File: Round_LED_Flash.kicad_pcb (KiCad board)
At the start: 4 copper layers, 84 x 84 mm, 65 parts, among them J1 USB4085-GF-A, J2 BATTERY, Q20 AO3401A, Q21 AO3401A, Q22 2N7002-7-F, Q23 2N7002-7-F, SW1 POWER, SW2 SHUTTER, U10 ESP32-C3-WROOM-02-N4, U6 TPS63070RNMR

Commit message: Preserve balanced supercapacitor charger draft before completion
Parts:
- removed C31, C33: 5F 2.7V, Capacitor_THT:CP_Radial_D10.0mm_P5.00mm
- removed R31, R32: 2.2k, Resistor_SMD:R_0603_1608Metric
- added C60: 4.7u 10V, Capacitor_SMD:C_0805_2012Metric, B.Cu at (130.0, 107.0)
- added C61: 2.2u 16V, Capacitor_SMD:C_0805_2012Metric, B.Cu at (126.0, 114.5)
- added Q30: AO3401A, Package_TO_SOT_SMD:SOT-23, B.Cu at (129.5, 112.0)
- added Q31: MMBT3904-7-F, Package_TO_SOT_SMD:SOT-23, B.Cu at (134.0, 113.0)
- added Q32: MMBT3904-7-F, Package_TO_SOT_SMD:SOT-23, B.Cu at (130.0, 120.0)
- added Q33: MMBT3904-7-F, Package_TO_SOT_SMD:SOT-23, F.Cu at (108.0, 134.0)
- added R52: 100k, Resistor_SMD:R_0603_1608Metric, B.Cu at (71.0, 92.0)
- added R53: 100k, Resistor_SMD:R_0603_1608Metric, B.Cu at (67.0, 103.0)
- added R60: 100k, Resistor_SMD:R_0603_1608Metric, B.Cu at (134.0, 105.0)
- added R61: 24k, Resistor_SMD:R_0603_1608Metric, B.Cu at (136.5, 109.0)
- added R62: 10k, Resistor_SMD:R_0603_1608Metric, B.Cu at (128.0, 108.5)
- added R63: 10k, Resistor_SMD:R_0603_1608Metric, B.Cu at (131.0, 115.5)
- added R64: 100k, Resistor_SMD:R_0603_1608Metric, B.Cu at (133.0, 119.0)
- added R65: 100k, Resistor_SMD:R_0603_1608Metric, F.Cu at (111.5, 137.0)
- added R66: 100k, Resistor_SMD:R_0603_1608Metric, B.Cu at (126.5, 123.0)
- added R67: 100k, Resistor_SMD:R_0603_1608Metric, B.Cu at (138.0, 111.5)
- added R68: 47k, Resistor_SMD:R_0603_1608Metric, B.Cu at (130.0, 123.0)
- added R69: 47k, Resistor_SMD:R_0603_1608Metric, F.Cu at (108.0, 137.0)
- added U30: LTC3225EDDB#TRMPBF, Package_DFN_QFN:DFN-10-1EP_2x3mm_P0.5mm_EP0.64x2.4mm, B.Cu at (133.5, 109.0)
- Q22, Q23: value 2N7002-7-F -> MMBT3904-7-F
- moved C32 13.4 mm to (128.7, 115.9)
- moved R50 2.00 mm to (71.0, 90.0)
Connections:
- Q22 pad 1: /LOGIC_PG -> /SENSE_BASE_0
- Q23 pad 1: /LOGIC_PG -> /SENSE_BASE_1

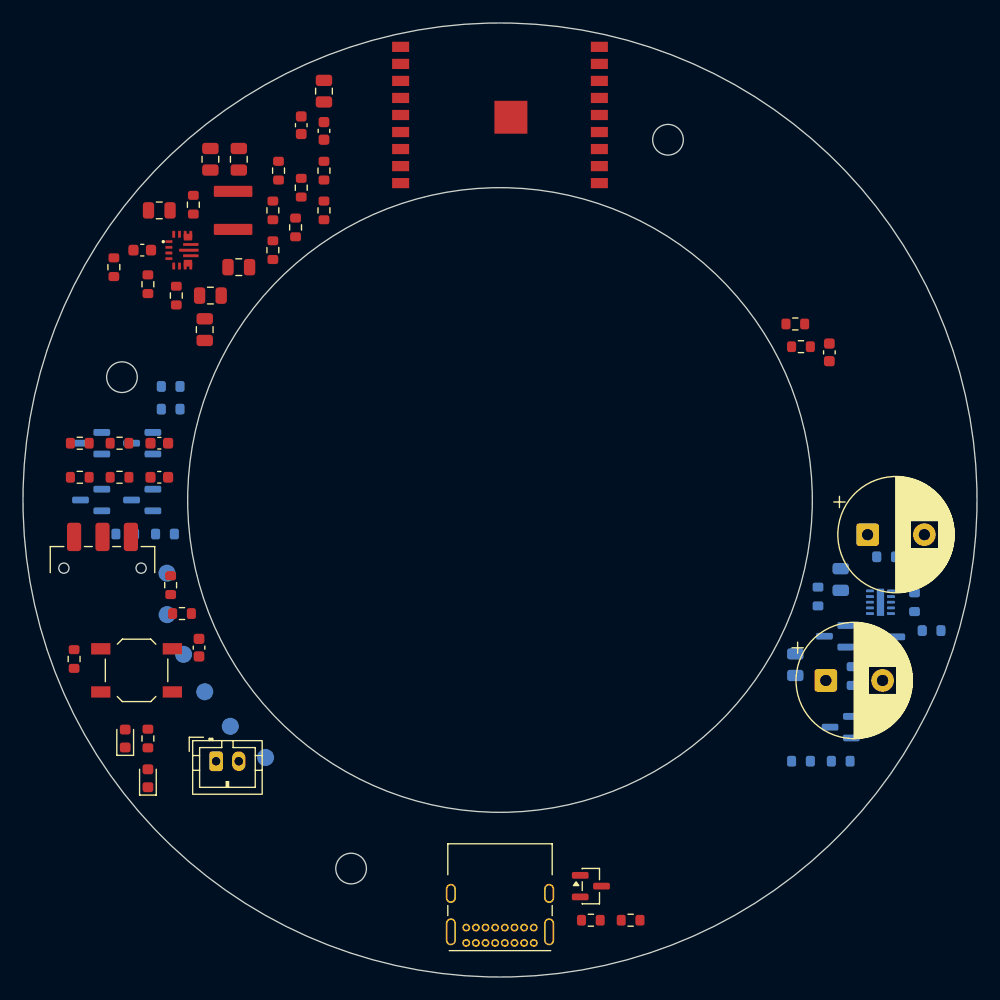
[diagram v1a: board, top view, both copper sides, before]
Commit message: Complete prototype circuit candidate with protected power and bounded flash control
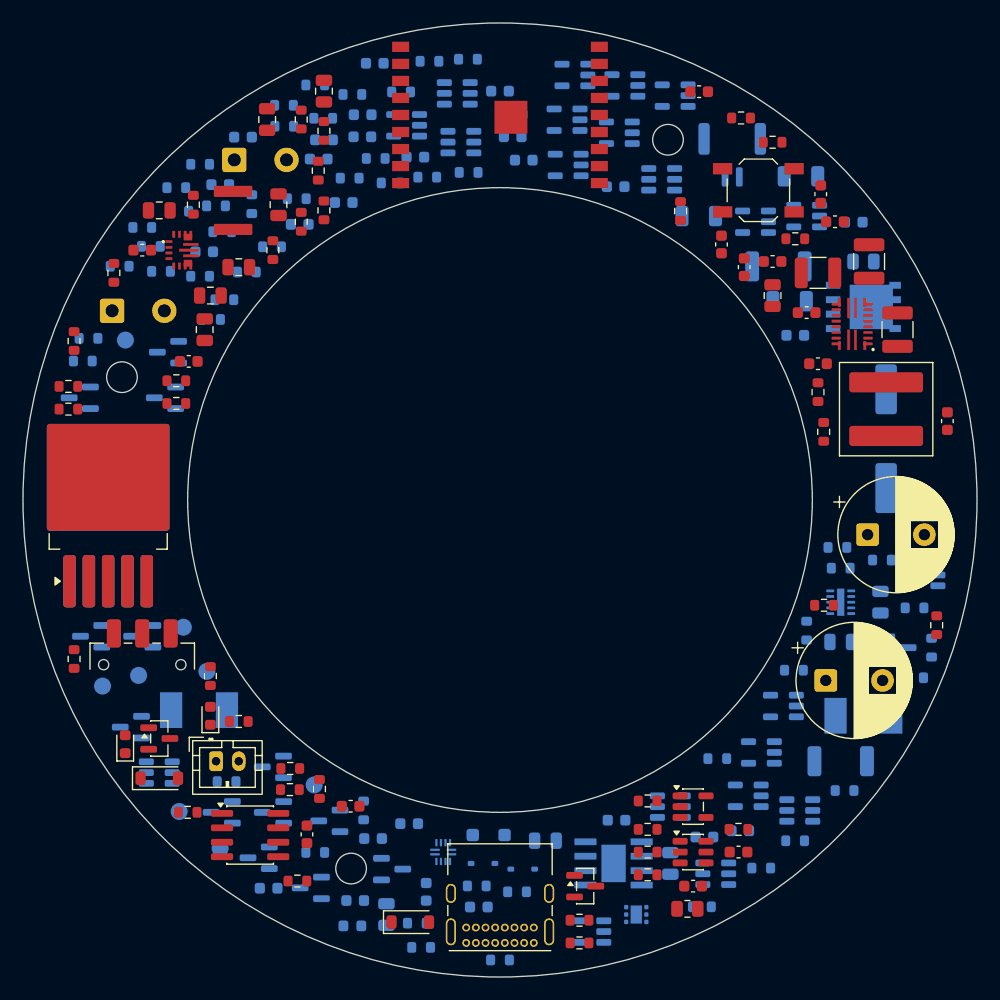
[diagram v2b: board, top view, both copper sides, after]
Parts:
- added C1: 100n, Capacitor_SMD:C_0603_1608Metric, B.Cu at (110.3, 128.2)
- added C140: 100n, Capacitor_SMD:C_0603_1608Metric, B.Cu at (84.5, 68.3)
- added C141: 100n, Capacitor_SMD:C_0603_1608Metric, B.Cu at (101.1, 68.0)
- added C142: 100n, Capacitor_SMD:C_0603_1608Metric, B.Cu at (77.4, 68.1)
- added C143: 100n, Capacitor_SMD:C_0603_1608Metric, B.Cu at (110.2, 72.4)
- added C144: 100n, Capacitor_SMD:C_0603_1608Metric, B.Cu at (89.0, 61.5)
- added C145: 100n, Capacitor_SMD:C_0603_1608Metric, B.Cu at (87.2, 135.3)
- added C146: 100n, Capacitor_SMD:C_0603_1608Metric, B.Cu at (100.0, 64.0)
- added C147: 100n, Capacitor_SMD:C_0603_1608Metric, B.Cu at (131.2, 75.5)
- added C148: 100n, Capacitor_SMD:C_0603_1608Metric, B.Cu at (98.1, 135.8)
- added C149: 100n, Capacitor_SMD:C_0603_1608Metric, B.Cu at (92.5, 69.8)
- added C150: 100n, Capacitor_SMD:C_0603_1608Metric, B.Cu at (82.4, 75.7)
- added C151: 100n, Capacitor_SMD:C_0603_1608Metric, B.Cu at (126.0, 85.5)
- added C152: 100n, Capacitor_SMD:C_0603_1608Metric, B.Cu at (118.0, 129.7)
- added C153: 100n, Capacitor_SMD:C_0603_1608Metric, B.Cu at (84.0, 70.0)
- added C155: 100n, Capacitor_SMD:C_0603_1608Metric, F.Cu at (121.0, 131.0)
- added C156: 100n, Capacitor_SMD:C_0603_1608Metric, F.Cu at (117.0, 134.0)
- added C162: 100n, Capacitor_SMD:C_0603_1608Metric, B.Cu at (86.2, 73.8)
- added C163: 100n, Capacitor_SMD:C_0603_1608Metric, B.Cu at (74.0, 78.1)
- added C2: 1u 50V, Capacitor_SMD:C_0805_2012Metric, B.Cu at (90.0, 136.5)
- added C230: 1u 10V, Capacitor_SMD:C_0603_1608Metric, B.Cu at (87.9, 68.0)
- added C231: 1u 10V, Capacitor_SMD:C_0603_1608Metric, B.Cu at (87.9, 66.1)
- added C236: 100n, Capacitor_SMD:C_0603_1608Metric, B.Cu at (102.1, 70.1)
- added C270: 22u 10V, Capacitor_SMD:C_1206_3216Metric, B.Cu at (125.5, 82.5)
- added C271: 22u 10V, Capacitor_SMD:C_1206_3216Metric, B.Cu at (126.5, 71.5)
- added C272: 22u 10V, Capacitor_SMD:C_1206_3216Metric, B.Cu at (117.5, 75.0)
- added C273: 100n, Capacitor_SMD:C_0603_1608Metric, F.Cu at (117.5, 64.0)
- added C274: 100n 50V, Capacitor_SMD:C_0603_1608Metric, F.Cu at (127.0, 83.5)
- added C275: 2.2u 10V, Capacitor_SMD:C_0805_2012Metric, F.Cu at (124.0, 82.0)
- added C276: 10n, Capacitor_SMD:C_0603_1608Metric, F.Cu at (121.5, 79.5)
- added C277: 33n, Capacitor_SMD:C_0603_1608Metric, F.Cu at (124.0, 79.0)
- added C278: 47p, Capacitor_SMD:C_0603_1608Metric, F.Cu at (129.5, 75.5)
- added C280: 10u 50V, Capacitor_SMD:C_1210_3225Metric, F.Cu at (135.0, 85.0)
- added C281: 10u 50V, Capacitor_SMD:C_1210_3225Metric, F.Cu at (132.5, 79.0)
- added C282: 10u 50V, Capacitor_SMD:C_1210_3225Metric, F.Cu at (128.0, 80.0)
- added C283: 100n 50V, Capacitor_SMD:C_0603_1608Metric, F.Cu at (128.0, 88.0)
- added C284: 120u 35V, Capacitor_SMD:CP_Elec_10x12.6, B.Cu at (134.0, 94.6)
- added C3: 1u 10V, Capacitor_SMD:C_0603_1608Metric, B.Cu at (93.5, 134.5)
- added C4: 100n, Capacitor_SMD:C_0603_1608Metric, B.Cu at (92.0, 128.5)
- added C5: 100n, Capacitor_SMD:C_0603_1608Metric, B.Cu at (79.6, 134.2)
- added C6: 4.7u 16V, Capacitor_SMD:C_0805_2012Metric, B.Cu at (115.0, 132.0)
- added C7: 100n 50V, Capacitor_SMD:C_0603_1608Metric, B.Cu at (88.8, 129.8)
- added C8: 10u 10V, Capacitor_SMD:C_0805_2012Metric, B.Cu at (104.0, 130.0)
- added C80: 100n, Capacitor_SMD:C_0603_1608Metric, B.Cu at (75.4, 72.2)
- added C9: 100n, Capacitor_SMD:C_0603_1608Metric, B.Cu at (121.2, 129.1)
- added D1: RED, LED_SMD:LED_0603_1608Metric, B.Cu at (87.0, 137.5)
- added D4: PESD5V0S1BA, Diode_SMD:D_SOD-323, B.Cu at (98.5, 132.0)
- added D5: PESD5V0S1BA, Diode_SMD:D_SOD-323, B.Cu at (102.0, 132.5)
- added D6: SMF4L6.0A, Diode_SMD:D_SOD-123F, B.Cu at (99.0, 129.5)
- added D60: 10V ZENER, Diode_SMD:D_SOD-123, F.Cu at (70.0, 124.5)
- added D70: GATE CLAMP, Diode_SMD:D_SOD-123, F.Cu at (92.1, 137.2)
- added F1: 2A FAST, Fuse:Fuse_Littelfuse-NANO2-451_453, B.Cu at (73.5, 118.5)
- added F2: 7A FAST, Fuse:Fuse_Littelfuse-NANO2-451_453, B.Cu at (132.0, 119.0)
- added J3: BM02B-GHS-TBT(LF)(SN), Connector_JST:JST_GH_BM02B-GHS-TBT_1x02-1MP_P1.25mm_Vertical, B.Cu at (120.4, 69.6)
- added J4: WARM COB, Connector_Wire:SolderWire-0.5sqmm_1x02_P4.6mm_D0.9mm_OD2.1mm, F.Cu at (65.8, 83.3)
- added J5: COOL COB, Connector_Wire:SolderWire-0.5sqmm_1x02_P4.6mm_D0.9mm_OD2.1mm, F.Cu at (76.6, 70.1)
- added L2: 1.5uH, Inductor_SMD:L_Coilcraft_XAL7030-152, F.Cu at (134.0, 92.0)
- added Q1: AO3400A, Package_TO_SOT_SMD:SOT-23, B.Cu at (80.0, 123.5)
- added Q2: AO3400A, Package_TO_SOT_SMD:SOT-23, B.Cu at (75.5, 127.5)
- added Q3: MMBT3904-7-F, Package_TO_SOT_SMD:SOT-23, B.Cu at (67.5, 120.0)
- added Q34: AO3400A, Package_TO_SOT_SMD:SOT-23, B.Cu at (70.8, 87.0)
- added Q35: MMBT3904-7-F, Package_TO_SOT_SMD:SOT-23, B.Cu at (85.0, 128.3)
- added Q60: AO4407A, Package_SO:SOIC-8_3.9x4.9mm_P1.27mm, F.Cu at (78.0, 129.5)
- added Q61: MMBT3904-7-F, Package_TO_SOT_SMD:SOT-23, F.Cu at (70.0, 121.0)
- added Q62: MMBT3904-7-F, Package_TO_SOT_SMD:SOT-23, B.Cu at (80.0, 127.5)
- added Q70: SiR800DP-T1-GE3, Package_SO:PowerPAK_SO-8_Single, B.Cu at (132.0, 83.0)
- added R1: 100, Resistor_SMD:R_0603_1608Metric, B.Cu at (75.5, 76.4)
- added R100: 4.7k, Resistor_SMD:R_0603_1608Metric, B.Cu at (83.7, 63.5)
- added R101: 4.7k, Resistor_SMD:R_0603_1608Metric, B.Cu at (125.9, 115.0)
- added R142: 165k, Resistor_SMD:R_0603_1608Metric, B.Cu at (130.0, 106.0)
- added R143: 147k, Resistor_SMD:R_0603_1608Metric, B.Cu at (133.6, 105.3)
- added R15: 2.2k, Resistor_SMD:R_0603_1608Metric, B.Cu at (77.7, 79.9)
- added R152: 100k, Resistor_SMD:R_0603_1608Metric, B.Cu at (63.8, 85.8)
- added R153: 10k, Resistor_SMD:R_0603_1608Metric, B.Cu at (81.0, 67.1)
- added R16: 22, Resistor_SMD:R_0603_1608Metric, B.Cu at (101.5, 134.5)
- added R162: 10k, Resistor_SMD:R_0603_1608Metric, B.Cu at (129.7, 104.2)
- added R163: 10k, Resistor_SMD:R_0603_1608Metric, B.Cu at (93.6, 71.6)
- added R164: 2.21M, Resistor_SMD:R_0603_1608Metric, B.Cu at (98.0, 134.0)
- added R165: 1M, Resistor_SMD:R_0603_1608Metric, B.Cu at (73.6, 70.4)
- added R17: 22, Resistor_SMD:R_0603_1608Metric, B.Cu at (100.0, 140.5)
- added R18: 10k, Resistor_SMD:R_0603_1608Metric, B.Cu at (136.5, 109.5)
- added R2: 1k, Resistor_SMD:R_0603_1608Metric, B.Cu at (69.3, 77.7)
- added R200: 137k, Resistor_SMD:R_0603_1608Metric, B.Cu at (84.4, 66.4)
- added R201: 240k, Resistor_SMD:R_0603_1608Metric, B.Cu at (86.8, 71.7)
- added R210: 357k, Resistor_SMD:R_0603_1608Metric, B.Cu at (97.2, 71.2)
- added R211: 146k, Resistor_SMD:R_0603_1608Metric, B.Cu at (87.0, 64.3)
- added R220: 100k, Resistor_SMD:R_0603_1608Metric, B.Cu at (71.8, 74.6)
- added R221: 100k, Resistor_SMD:R_0603_1608Metric, B.Cu at (93.8, 61.4)
- added R230: 2.49k, Resistor_SMD:R_0603_1608Metric, B.Cu at (91.3, 64.1)
- added R231: 2.49k, Resistor_SMD:R_0603_1608Metric, B.Cu at (136.5, 115.7)
- added R232: 4.7k, Resistor_SMD:R_0603_1608Metric, F.Cu at (72.5, 127.5)
- added R233: 2.2k, Resistor_SMD:R_0603_1608Metric, F.Cu at (81.5, 125.5)
- added R234: 2.2k, Resistor_SMD:R_0603_1608Metric, F.Cu at (77.0, 119.5)
- added R235: 100k, Resistor_SMD:R_0603_1608Metric, F.Cu at (82.2, 133.6)
- added R236: 10k, Resistor_SMD:R_0603_1608Metric, B.Cu at (90.4, 72.1)
- added R237: 10k, Resistor_SMD:R_0603_1608Metric, B.Cu at (97.2, 61.2)
- added R238: 56k, Resistor_SMD:R_0603_1608Metric, B.Cu at (75.0, 74.1)
- added R239: 261k, Resistor_SMD:R_0603_1608Metric, F.Cu at (113.0, 129.0)
- added R240: 100k, Resistor_SMD:R_0603_1608Metric, F.Cu at (113.0, 131.0)
- added R241: 10M, Resistor_SMD:R_0603_1608Metric, F.Cu at (113.0, 133.0)
- added R242: 10k, Resistor_SMD:R_0603_1608Metric, F.Cu at (121.0, 129.0)
- added R270: 0.010 0.5W, Resistor_SMD:R_0805_2012Metric, B.Cu at (132.0, 79.0)
- added R271: 162k, Resistor_SMD:R_0603_1608Metric, F.Cu at (128.0, 90.5)
- added R272: 10k, Resistor_SMD:R_0603_1608Metric, F.Cu at (128.5, 94.0)
- added R273: 1k, Resistor_SMD:R_0603_1608Metric, F.Cu at (113.0, 126.5)
- added R274: 100k, Resistor_SMD:R_0603_1608Metric, F.Cu at (107.0, 137.0)
- added R275: 120k, Resistor_SMD:R_0603_1608Metric, F.Cu at (126.0, 77.0)
- added R276: 22k 0.125W, Resistor_SMD:R_0805_2012Metric, F.Cu at (116.5, 136.0)
- added R3: 47k, Resistor_SMD:R_0603_1608Metric, B.Cu at (93.1, 139.4)
- added R4: 887k, Resistor_SMD:R_0603_1608Metric, B.Cu at (123.0, 132.4)
- added R5: 10k, Resistor_SMD:R_0603_1608Metric, B.Cu at (92.7, 137.3)
- added R6: 150k, Resistor_SMD:R_0603_1608Metric, B.Cu at (70.2, 79.9)
- added R7: 10k, Resistor_SMD:R_0603_1608Metric, B.Cu at (74.6, 84.1)
- added R70: 100k, Resistor_SMD:R_0603_1608Metric, B.Cu at (89.1, 69.9)
- added R71: 100k, Resistor_SMD:R_0603_1608Metric, B.Cu at (130.3, 125.6)
- added R72: 100 0.5W, Resistor_SMD:R_2010_5025Metric, B.Cu at (130.0, 123.0)
- added R73: 100 0.5W, Resistor_SMD:R_2010_5025Metric, B.Cu at (124.5, 79.4)
- added R8: 100k, Resistor_SMD:R_0603_1608Metric, B.Cu at (75.7, 82.4)
- added R80: 6.49k, Resistor_SMD:R_0603_1608Metric, B.Cu at (83.7, 131.0)
- added R81: 1M, Resistor_SMD:R_0603_1608Metric, B.Cu at (119.1, 122.8)
- added R82: 1M, Resistor_SMD:R_0603_1608Metric, B.Cu at (126.0, 130.0)
- added R83: 100k, Resistor_SMD:R_0603_1608Metric, B.Cu at (79.9, 77.7)
- added R84: 100k, Resistor_SMD:R_0603_1608Metric, B.Cu at (73.6, 80.3)
- added R9: 4.02k, Resistor_SMD:R_0603_1608Metric, B.Cu at (117.8, 135.8)
- added TP7: CAP_BANK, TestPoint:TestPoint_Pad_D1.5mm, B.Cu at (72.1, 111.2)
- added TP8: CAP_MID, TestPoint:TestPoint_Pad_D1.5mm, B.Cu at (67.0, 85.9)
- added U1: DW01A, Package_TO_SOT_SMD:SOT-23-6, B.Cu at (70.0, 124.0)
- added U2: TLV76033DBZR, Package_TO_SOT_SMD:SOT-23, B.Cu at (90.5, 132.5)
- added U3: TUSB320LAIRWBR, Package_DFN_QFN:Texas_X2QFN-12_1.6x1.6mm_P0.4mm, B.Cu at (95.0, 131.0)
- added U4: SN74LVC1G04DBVR, Package_TO_SOT_SMD:SOT-23-5, B.Cu at (108.0, 138.0)
- added U40: LTC6993CS6-1#TRMPBF, Package_TO_SOT_SMD:SOT-23-6, B.Cu at (114.2, 71.8)
- added U41: LTC6993CS6-1#TRMPBF, Package_TO_SOT_SMD:SOT-23-6, B.Cu at (96.6, 68.5)
- added U42: TLV3011BIDBVR, Package_TO_SOT_SMD:SOT-23-6, B.Cu at (96.2, 64.2)
- added U43: TLV3011BIDBVR, Package_TO_SOT_SMD:SOT-23-6, B.Cu at (137.4, 106.6)
- added U44: SN74LVC1G08DBVR, Package_TO_SOT_SMD:SOT-23-5, B.Cu at (122.5, 75.5)
- added U45: SN74LVC1G04DBVR, Package_TO_SOT_SMD:SOT-23-5, B.Cu at (111.0, 63.5)
- added U46: SN74LVC1G08DBVR, Package_TO_SOT_SMD:SOT-23-5, B.Cu at (110.5, 67.7)
- added U47: SN74LVC1G08DBVR, Package_TO_SOT_SMD:SOT-23-5, B.Cu at (91.8, 67.0)
- added U48: SN74LVC1G08DBVR, Package_TO_SOT_SMD:SOT-23-5, B.Cu at (123.0, 122.2)
- added U49: SN74LVC1G08DBVR, Package_TO_SOT_SMD:SOT-23-5, B.Cu at (125.0, 118.1)
- added U5: TPS25200DRVR, Package_SON:WSON-6-1EP_2x2mm_P0.65mm_EP1x1.6mm, B.Cu at (112.0, 136.5)
- added U50: SN74LVC1G08DBVR, Package_TO_SOT_SMD:SOT-23-5, B.Cu at (106.6, 62.6)
- added U51: SN74LVC1G08DBVR, Package_TO_SOT_SMD:SOT-23-5, B.Cu at (106.0, 70.5)
- added U52: SN74LVC1G08DBVR, Package_TO_SOT_SMD:SOT-23-5, B.Cu at (105.9, 66.5)
- added U53: SN74LVC1G08DBVR, Package_TO_SOT_SMD:SOT-23-5, B.Cu at (115.4, 64.4)
- added U54: TPS3808G33DBVR, Package_TO_SOT_SMD:SOT-23-6, B.Cu at (126.4, 127.3)
- added U55: TLV3011BIDBVR, Package_TO_SOT_SMD:SOT-23-6, F.Cu at (117.0, 131.0)
- added U56: SN74LVC1G08DBVR, Package_TO_SOT_SMD:SOT-23-5, F.Cu at (117.0, 127.0)
- added U60: CAT4101TV-T75, Package_TO_SOT_SMD:TO-263-5_TabPin3, F.Cu at (65.5, 99.5)
- added U61: CAT4101TV-T75, Package_TO_SOT_SMD:TO-263-5_TabPin3, B.Cu at (65.5, 99.5)
- added U62: SN74LVC1G125DBVR, Package_TO_SOT_SMD:SOT-23-5, B.Cu at (121.9, 126.0)
- added U63: SN74LVC1G125DBVR, Package_TO_SOT_SMD:SOT-23-5, B.Cu at (127.0, 75.0)
- added U7: TP4056-42-ESOP8, Round_LED_Flash:TP4056_TopPower_ESOP8, B.Cu at (110.0, 132.0)
- added U70: MP3435GL-Z, Round_LED_Flash:MP3435_QFN20_3x4, F.Cu at (131.0, 84.5)
- added U8: TLV3011BIDBVR, Package_TO_SOT_SMD:SOT-23-6, B.Cu at (115.0, 127.0)
- added U9: TPS3808G30DBVR, Package_TO_SOT_SMD:SOT-23-6, B.Cu at (119.0, 132.9)
- D2: value BLUE -> AMBER BLE
- R12: value 10k -> 4.7k
- R13: value 10k -> 100k
- R14: value 100k -> 1M
- TP3: value UART_TX -> UART_TX_EXT
- TP4: value UART_RX -> UART_RX_EXT
- moved R65 71.3 mm to (121.2, 66.4)
- moved R64 71.0 mm to (78.1, 74.0)
- moved R22 70.4 mm to (138.5, 111.0)
- moved SW2 69.2 mm to (122.8, 72.7)
- moved R66 66.5 mm to (82.1, 73.5)
- moved R60 66.3 mm to (81.0, 65.2)
- moved C20 60.5 mm to (139.4, 93.1)
- moved R67 58.5 mm to (101.2, 66.0)
- moved Q31 54.9 mm to (83.3, 134.2)
- moved R68 54.1 mm to (75.9, 124.8)
- moved Q32 52.5 mm to (78.8, 131.5)
- moved R14 50.1 mm to (115.9, 74.6)
- moved C21 46.1 mm to (128.2, 73.1)
- moved R62 44.2 mm to (88.0, 127.3)
- moved C24 33.5 mm to (86.8, 127.0)
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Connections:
- net /STRAP2 renamed /TRIG_REQ
- J1 pad A5: /CC1 -> /CC1_RAW
- J1 pad B5: /CC2 -> /CC2_RAW
- TP3 pad 1: /UART_TX -> /UART_TX_EXT
- TP4 pad 1: /UART_RX -> /UART_RX_EXT
- U10 pad 6: /HW_OK -> /TRIGGER_ALLOWED
- U6 pad 1: /BAT_PROT -> /LOGIC_PS_SYNC

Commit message: Correct service bleed and ADC leakage; refine converter and decoupling placement
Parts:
- added R74: 330 0.25W, Resistor_SMD:R_1206_3216Metric, B.Cu at (126.7, 72.3)
- R27, R28, R29, R30: value 100k -> 22k
- moved C145 71.6 mm to (101.9, 65.2)
- moved C152 68.2 mm to (102.8, 63.2)
- moved C80 65.5 mm to (110.9, 127.2)
- moved C236 62.2 mm to (122.5, 128.8)
- moved C162 59.3 mm to (119.7, 122.8)
- moved R50 57.3 mm to (127.0, 86.8)
- moved C149 56.0 mm to (82.8, 125.0)
- moved C147 52.4 mm to (79.6, 65.7)
- moved SW2 51.7 mm to (123.6, 124.5)
- moved R153 47.6 mm to (125.4, 84.1)
- moved C1 43.3 mm to (67.6, 121.0)
- moved U49 41.2 mm to (85.0, 128.3)
- moved C143 40.2 mm to (133.3, 105.3)
- moved Q3 37.9 mm to (74.3, 82.7)
- moved U63 37.6 mm to (89.6, 71.3)
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
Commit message: Update Round LED Flash schematic, layout, routing scripts, and documentation
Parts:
- U9: value TPS3808G30DBVR -> TPS3808G33DBVR
- moved R270 8.60 mm to (137.0, 86.0), turned to 90 degrees
- moved C275 4.47 mm to (129.5, 79.0), turned to 0 degrees
- moved Q70 3.00 mm to (132.0, 86.0)
- moved C278 1.03 mm to (129.2, 77.0)
- moved C284 0.98 mm to (134.4, 95.5), turned to 0 degrees
- turned R272 to -90 degrees
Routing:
- net /3V3: track 0.00 -> 419.4 mm, vias 0 -> 47
- net /BAT_PROT: track 0.00 -> 239.5 mm, vias 0 -> 21
- net /BOOST_OUT: track 0.00 -> 179.9 mm, vias 0 -> 16
- net /VBUS_RAW: track 0.00 -> 133.6 mm, vias 0 -> 9
- net /CAP_BANK: track 0.00 -> 129.5 mm, vias 0 -> 9
- net /USB_5V: track 0.00 -> 105.8 mm, vias 0 -> 8
- net /LED_ANODES: track 0.00 -> 72.7 mm, vias 0 -> 1
- net /LED_C_K: track 0.00 -> 47.3 mm, vias 0 -> 3
- net /CAP_MID: track 0.00 -> 25.3 mm, vias 0 -> 1
- net /LED_W_K: track 0.00 -> 24.6 mm, vias 0 -> 2
- net /CELL_N_RAW: track 0.00 -> 18.7 mm, vias 0 -> 2
- net /BOOST_INPUT: track 0.00 -> 15.6 mm, vias 0 -> 2
- net /CELL_FET_COMMON: track 0.00 -> 12.8 mm, vias 0 -> 2
- net /BOOST_SENSE: track 0.00 -> 9.75 mm, vias 0 -> 1
- net /BOOST_FB: track 0.00 -> 8.70 mm
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- added copper zone on In1.Cu, net /GND
